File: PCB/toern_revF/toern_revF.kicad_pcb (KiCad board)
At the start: 4 copper layers, 160 x 71 mm, 92 parts, among them J1 AudioJack3_Switch, J10 Conn_01x02, J11 Conn_01x05, J11.5 Conn_01x05, J12 Conn_01x05, J13 Conn_01x05, J14 Conn_01x05, J15 Conn_01x05, J16 BATTERY, J17 AudioJack3_Ground, J3 AudioJack3_Ground, J4 USB_C_Receptacle_USB2.0, J5 AudioJack3_Switch, J6 AudioJack3_Switch, J7 AudioJack3_Switch, J8 Micro_SD_Card, J9 Conn_01x03, Q1 DMG3415, SW1 EG2219, U1 SPX3819M5-L-3-3, U10 01x05 Connector_PinSocket_2.5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, U11 01x05 Connector_PinSocket_2.5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, U12 01x05 Connector_PinSocket_2.5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, U13 PAM8403D, U2 SPX3819M5-L-1-8, U3 SGTL5000XNBA3, U4 TLP2361V4_E, U5 74LVC2G14, U6 Teensy4.1, U7 SPX3819M5-L-3-3, U8 MCP73831-3-OT, U9 01x05 Connector_PinSocket_2.5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

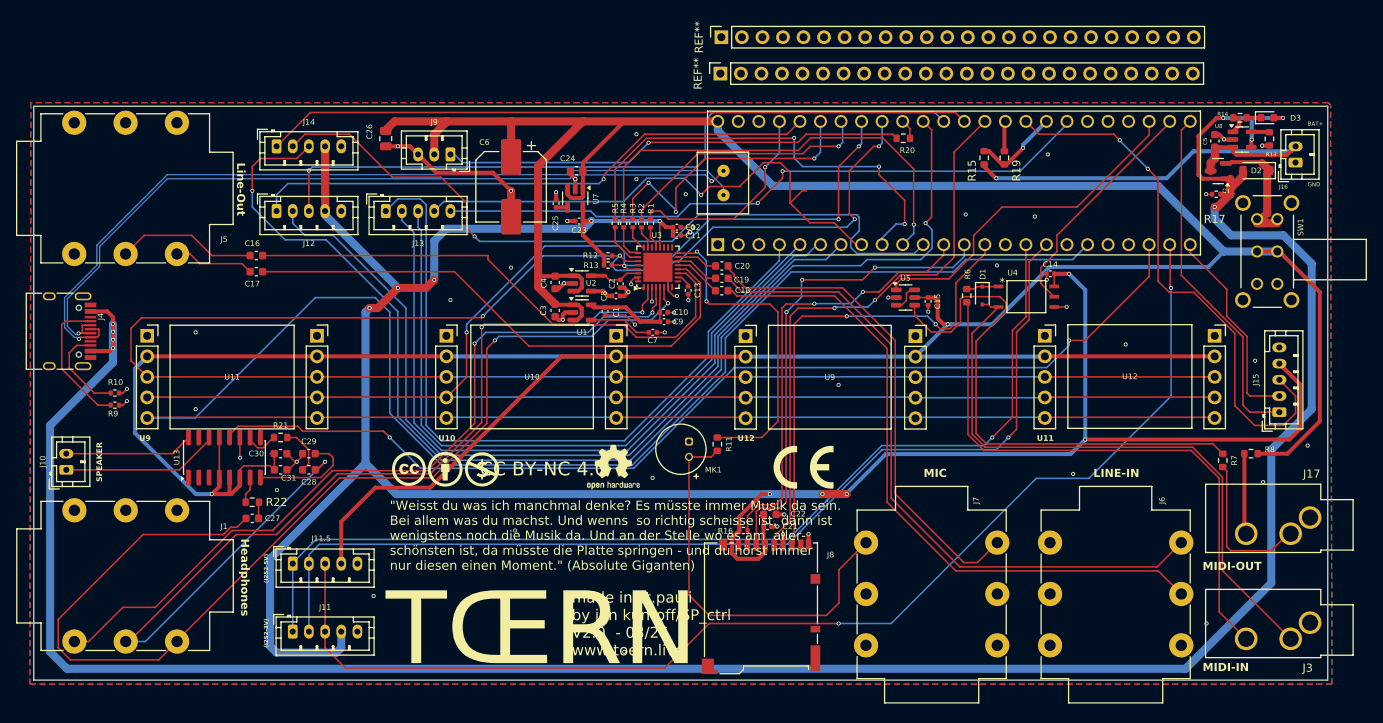
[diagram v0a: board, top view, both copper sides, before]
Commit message: pcb: fixing thermal relief
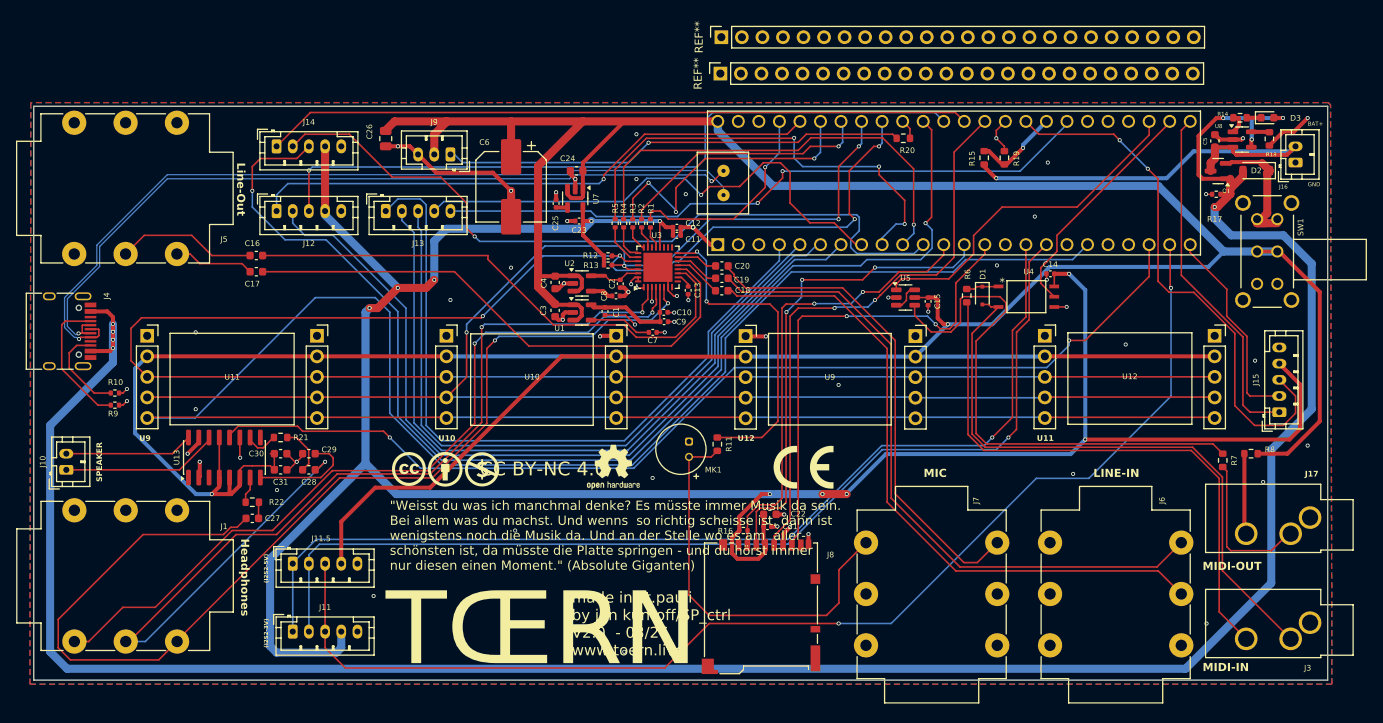
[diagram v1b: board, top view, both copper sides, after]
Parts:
- renumbered REF** to LOGOOPENHARDWARE
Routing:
- net GND: track 79.9 -> 101.7 mm, vias 57 -> 60
- net 6_OUT1D: track 66.0 -> 63.4 mm
